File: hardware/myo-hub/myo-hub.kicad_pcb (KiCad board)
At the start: 2 copper layers, 57.5 x 57 mm, 44 parts, among them IC1 AD4130-8BCPZ-RL7, J1 Conn_01x03, J10 Conn_01x03, J11 Conn_01x03, J12 Conn_01x03, J13 Conn_01x03, J14 Conn_01x03, J15 Conn_01x03, J16 Conn_01x03, J2 Conn_01x03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

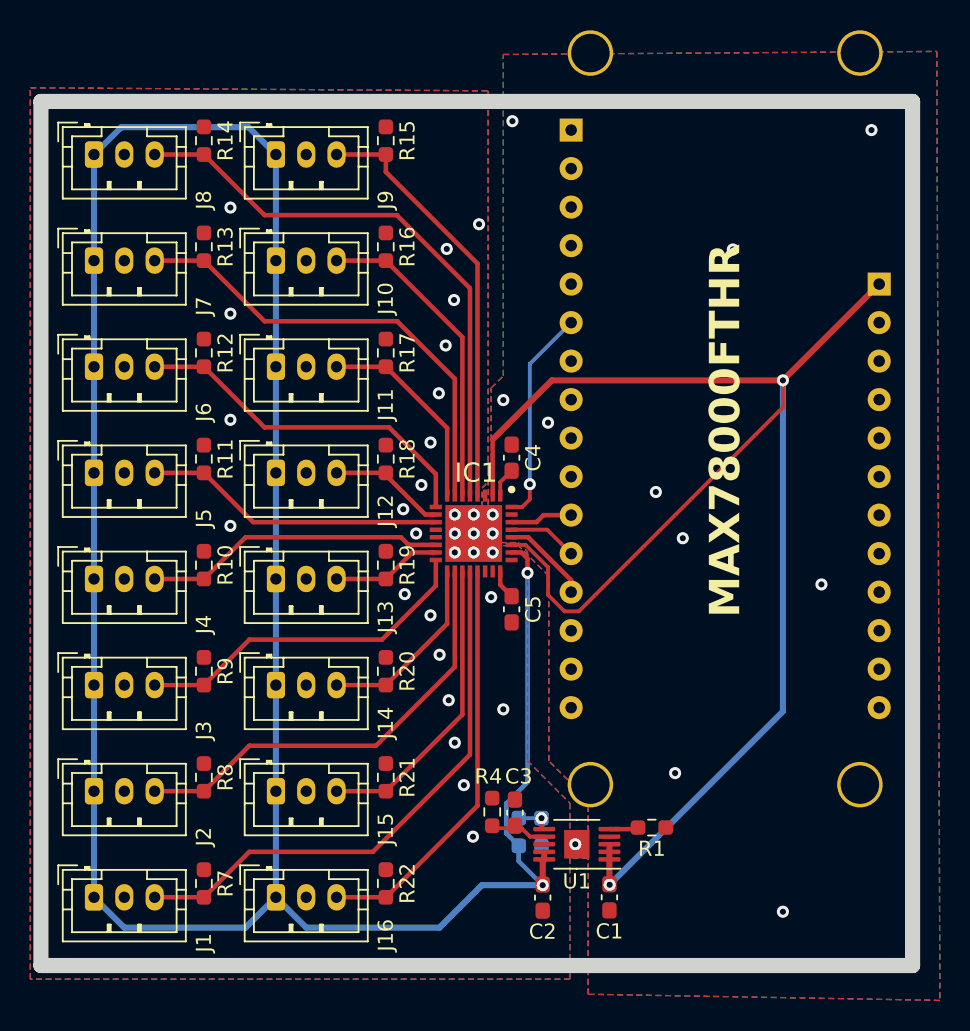
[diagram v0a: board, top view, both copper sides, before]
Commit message: Change ADC to AD7124-8
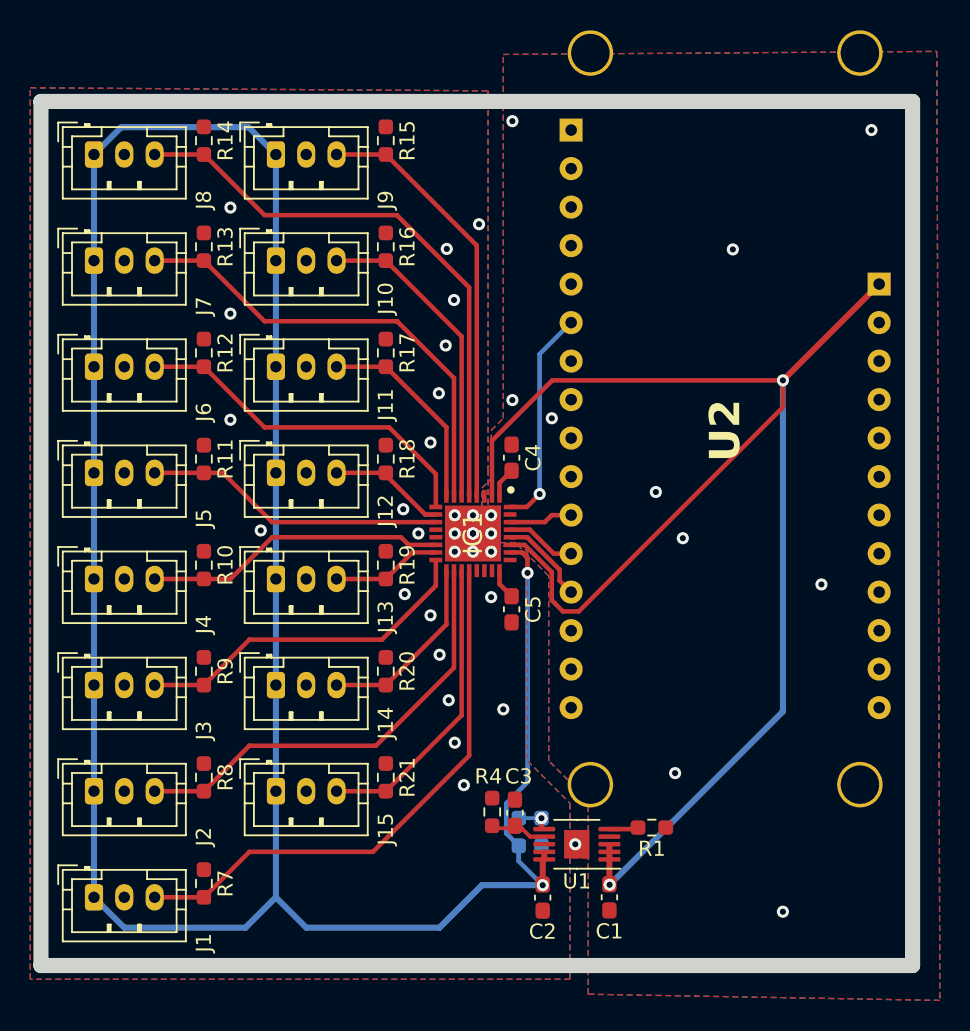
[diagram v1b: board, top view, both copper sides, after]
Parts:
- removed J16: Conn_01x03, Connector_JST:JST_PH_B3B-PH-K_1x03_P2.00mm_Vertical
- removed R22: 1M, Resistor_SMD:R_0603_1608Metric_Pad0.98x0.95mm_HandSolder
- IC1: value AD4130-8BCPZ-RL7 -> AD7124-8BBCPZ-RL7; footprint myo-hub:QFN50P500X500X80-33N-D -> myo-hub:QFN50P500X500X100-33N-D
- moved IC1 0.05 mm to (119.0, 83.0)
- renumbered MAX78000FTHR to U2
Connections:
- IC1 pad 21: V15 -> GND
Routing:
- net V15: track 27.3 -> 0.00 mm
- net GND: vias 42 -> 41

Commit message: Mainboard silkscreen, ground vias, routing tweaks
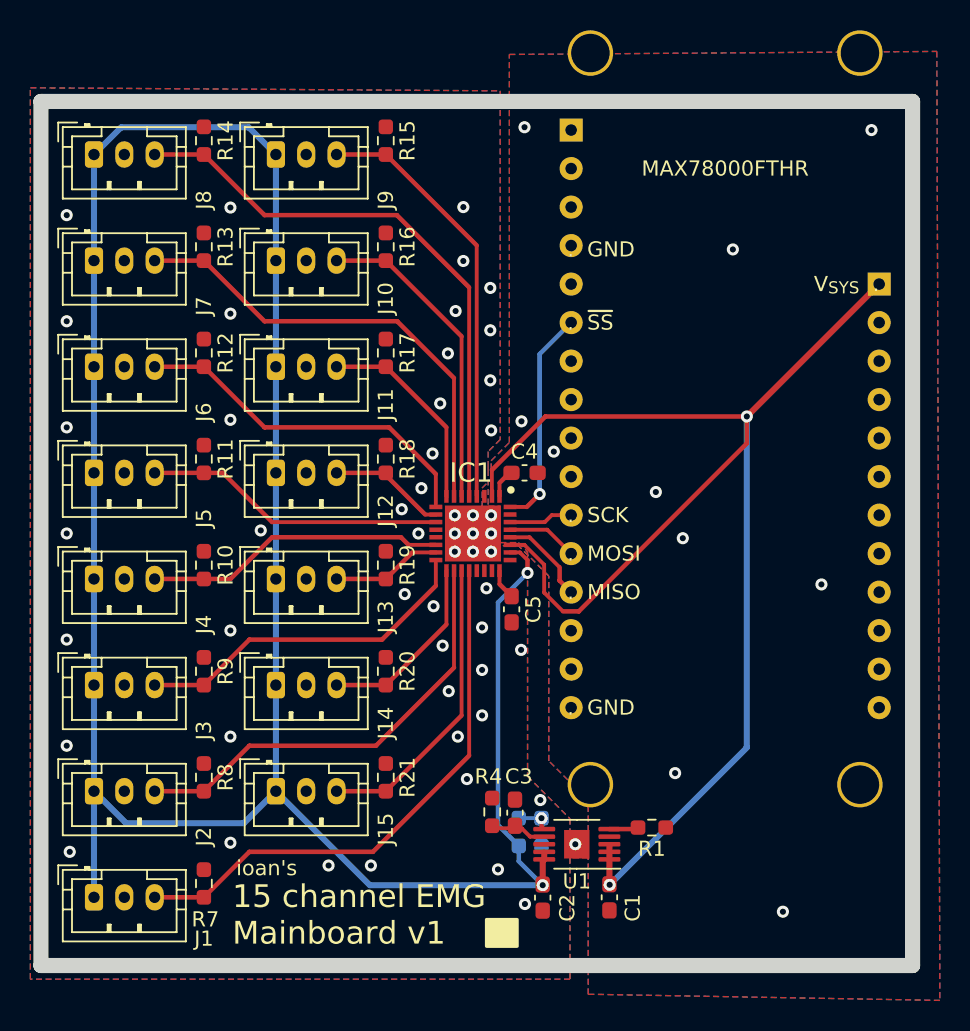
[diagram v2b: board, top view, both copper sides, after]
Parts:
- moved C4 1.31 mm to (122.4, 79.0), turned to 180 degrees
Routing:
- net VCC: track 102.3 -> 94.5 mm
- net VDDA: track 171.2 -> 165.3 mm
- net GND: vias 41 -> 63
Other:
- board text added: ". GND"
- board text added: ". MISO"
- board text added: ". MOSI"
- board text added: ". SCK"
- board text added: ". ~{SS}"
- board text added: "15 channel EMG Mainboard v1"
- board text added: "MAX78000FTHR"
- board text added: "V_{SYS} ."
- board text added: "ioan's"

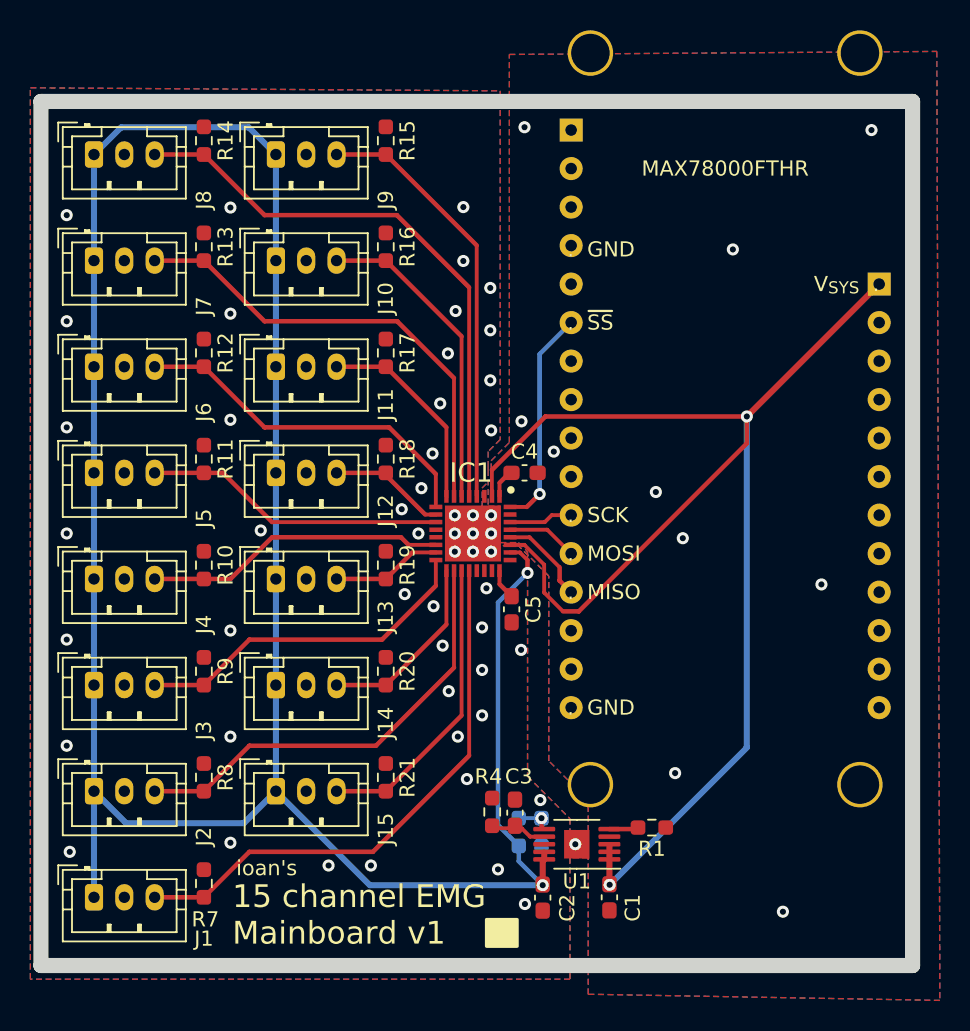
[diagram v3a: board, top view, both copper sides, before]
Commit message: Add pseudo-differential reference circuit
This in turn enables us to use the PGAs without saturating them.

With a zero reference, we can only use gain=1, because even gain=2
would result in a AVDD/2*2 = AVDD voltage at the PGA's output with
zero! input.
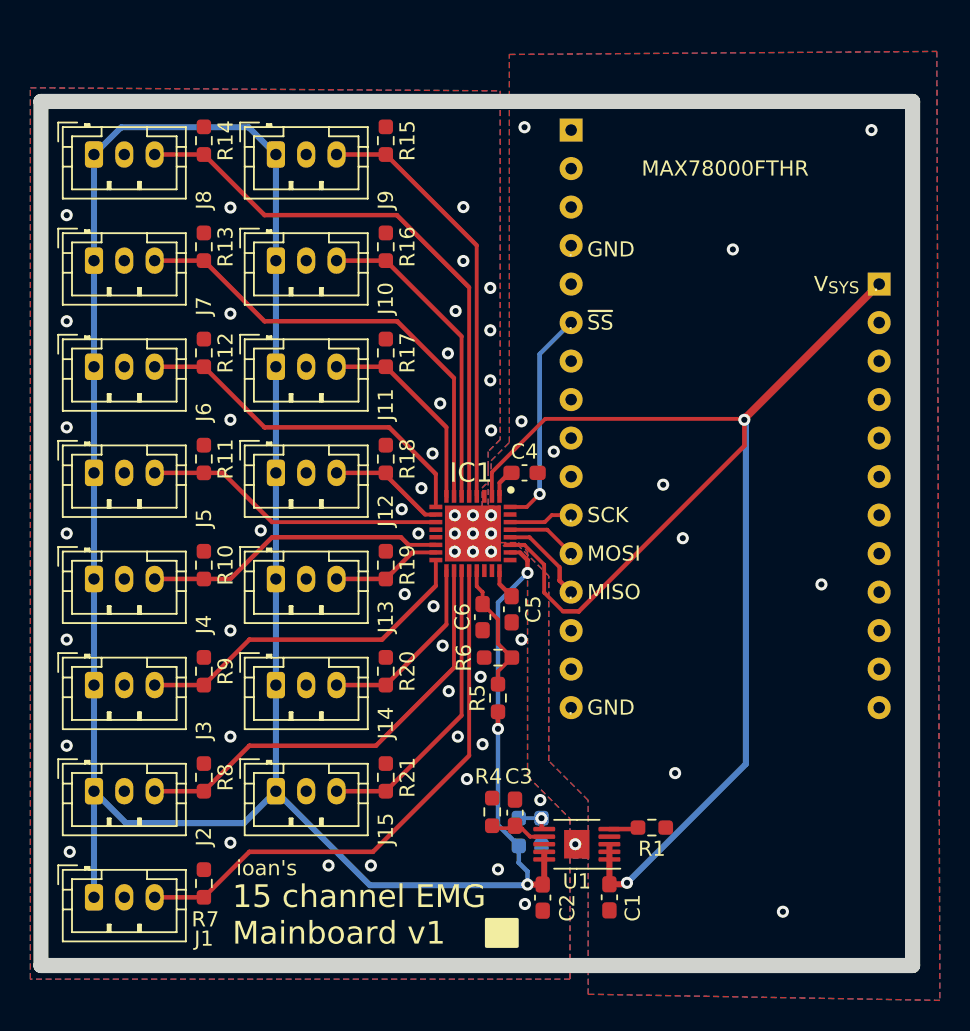
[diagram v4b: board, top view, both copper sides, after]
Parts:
- added C6: 0.1uF, Capacitor_SMD:C_0603_1608Metric_Pad1.08x0.95mm_HandSolder, F.Cu at (119.6, 88.5)
- added R5: 500k 1%, Resistor_SMD:R_0603_1608Metric_Pad0.98x0.95mm_HandSolder, F.Cu at (120.7, 93.9)
- added R6: 500k 1%, Resistor_SMD:R_0603_1608Metric_Pad0.98x0.95mm_HandSolder, F.Cu at (120.7, 91.2)
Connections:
- IC1 pad 21: GND -> COM
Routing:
- net COM: track 0.00 -> 8.83 mm
- net VDDA: track 165.3 -> 165.9 mm, vias 2 -> 3
- net GND: vias 63 -> 61

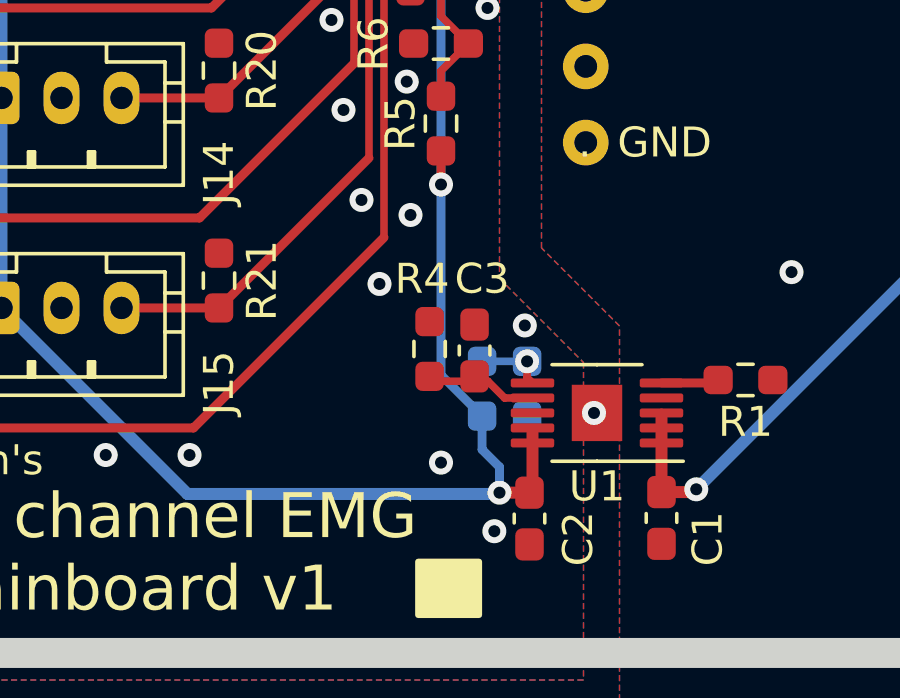
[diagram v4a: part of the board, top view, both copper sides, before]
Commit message: Move all components to primary side
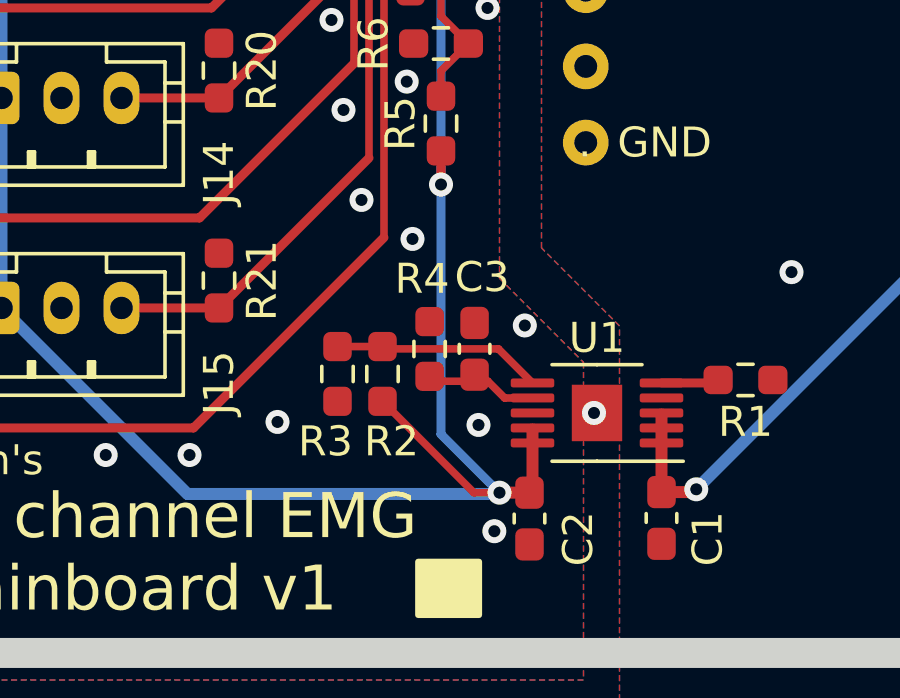
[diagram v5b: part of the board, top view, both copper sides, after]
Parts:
- R2, R3: moved to F.Cu
- moved R3 6.34 mm to (117.2, 102.2)
- moved R2 3.36 mm to (118.7, 102.2)
- moved C3 0.05 mm to (121.8, 101.4)
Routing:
- net VDDA: track 165.9 -> 171.2 mm
- net Net-(U1-PGFB): track 2.25 -> 7.00 mm, vias 1 -> 0
